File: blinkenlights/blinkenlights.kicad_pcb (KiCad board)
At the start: 4 copper layers, 160 x 100 mm, 169 parts, among them J201 Conn_03x32_Row_Letter_First, J301 Conn_01x01_Female, J302 Conn_01x01_Female, J303 Conn_01x01_Female, J304 Conn_01x01_Female, J501 Conn_ARM_SWD, J502 Conn_02x03_Odd_Even, SW101 Black, SW102 Orang, U104 74AUC2G07, U106 74HC2G14, U301 BD9C301FJ, U303 AMS1117-3.3, U401 74HC244, U402 74AUC2G34, U501 ATSAM4S8CB-AN, U502 PCA9306DP, U601 SN74LVCH16T245, U602 SN74LXC8T245, U603 SN74LVC2T45, U604 SN74LVC2T45, U605 SN74LVC2T45, U606 SN74LVCH16T245, U607 SN74LXC8T245, U608 74LVC2G06, U609 74LVC2G06, U610 74LVC2G06, U611 74LVC2G06

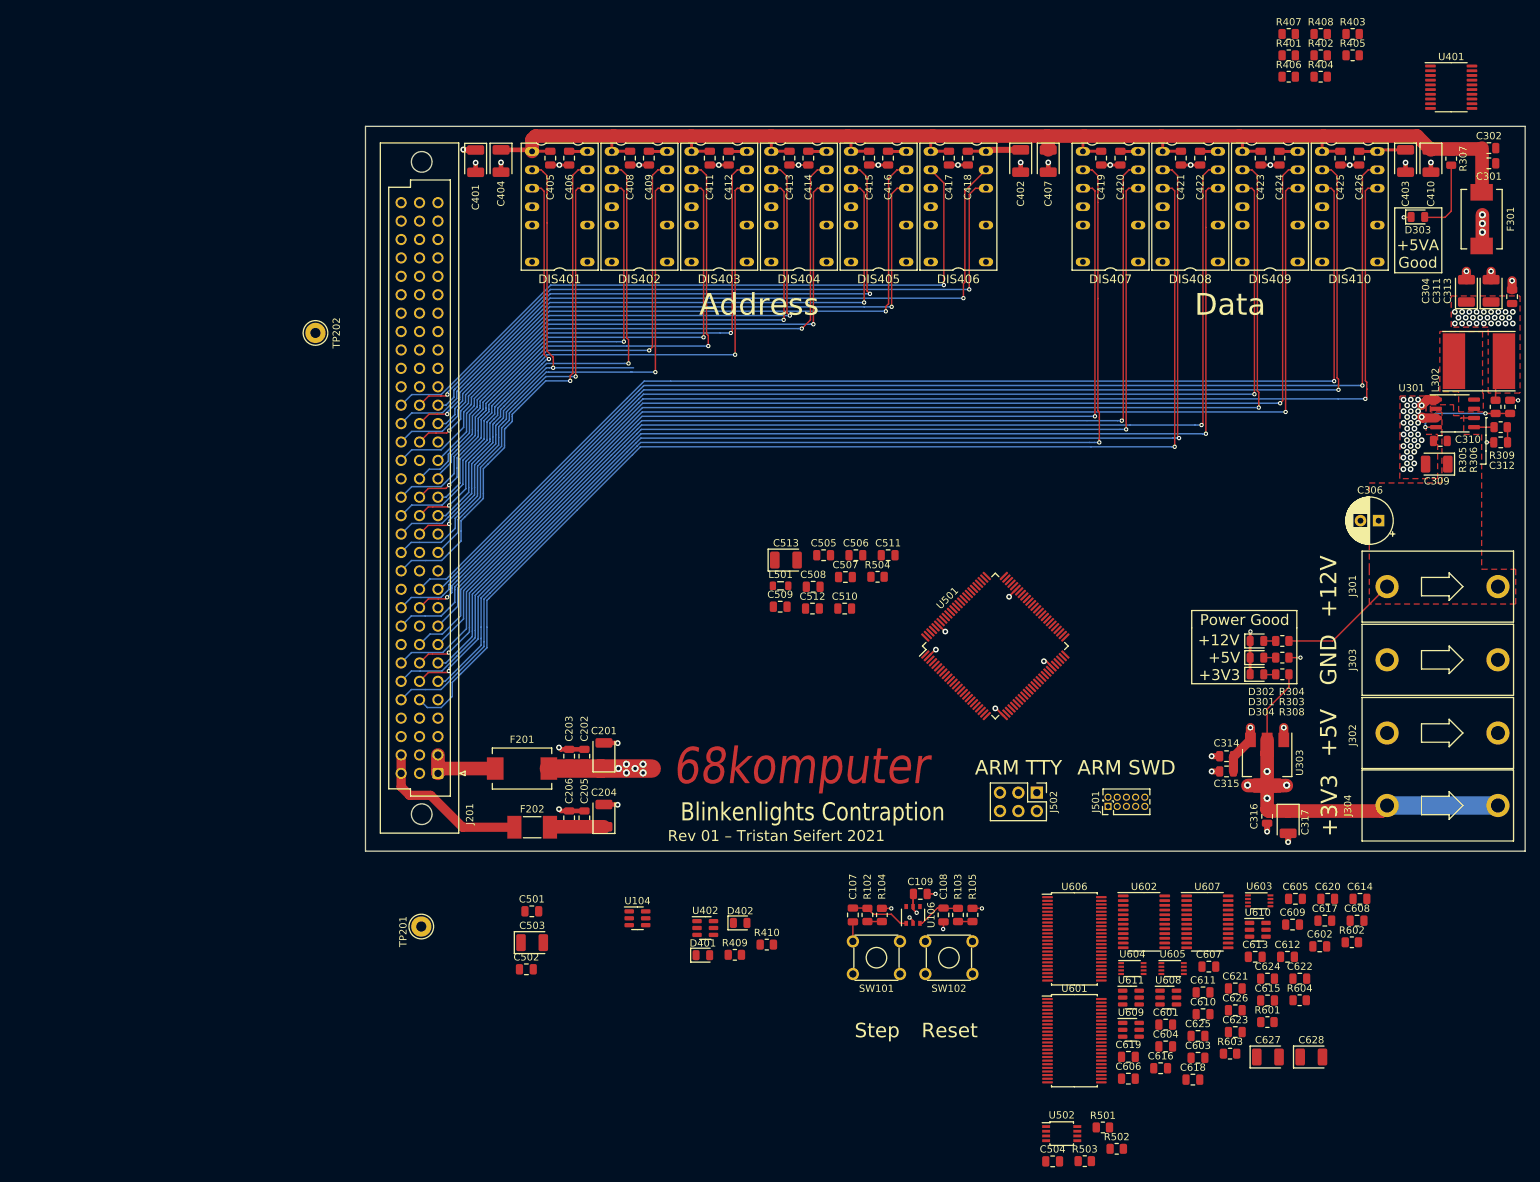
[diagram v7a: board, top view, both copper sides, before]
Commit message: Get rid of CPU on blinkenlights board
- We don't really care for having a full processor chilling on this
  board more than we do about being able to do a few bus transactions
  (to do fun stuff like flashing the boot ROMs) so we're going to put a
  bunch of SPI IO expanders instead; this should allow us to somewhat
  recreate bus cycles.

  We'll have to implement the run/halt/single step controls with
  dedicated logic though.
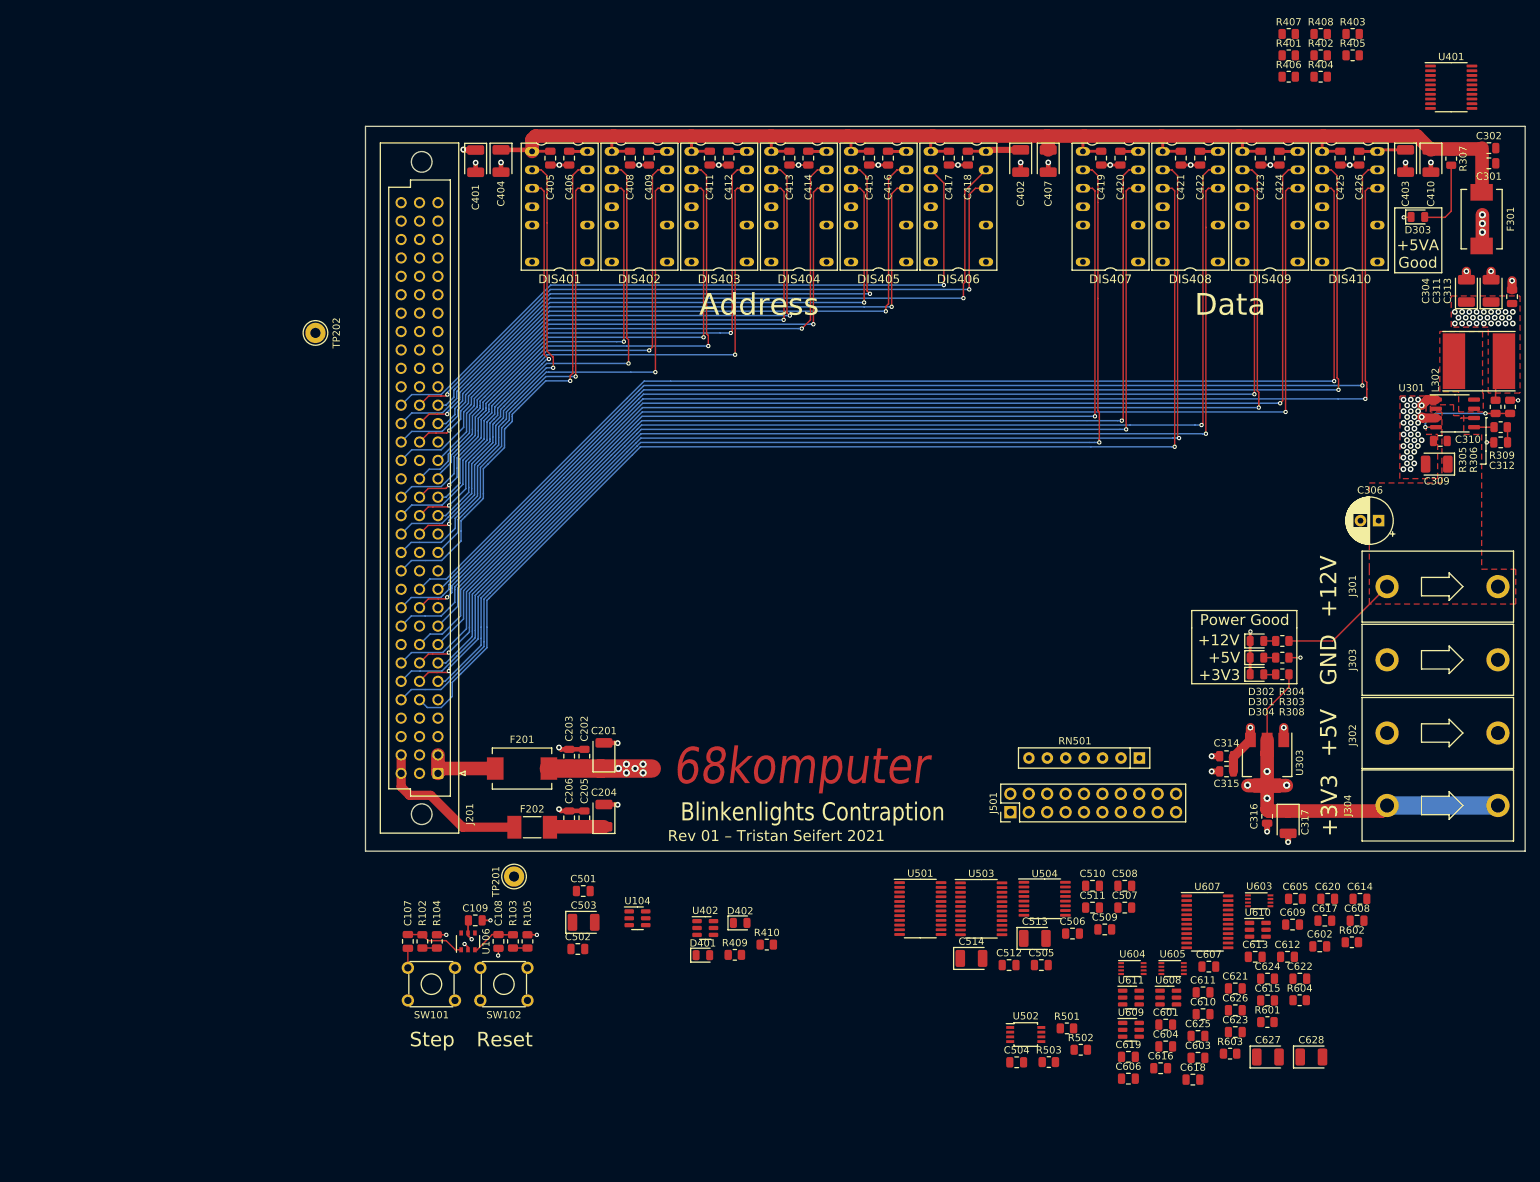
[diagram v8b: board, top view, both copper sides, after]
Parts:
- removed J502: Conn_02x03_Odd_Even, Connector_PinHeader_2.54mm:PinHeader_2x03_P2.54mm_Vertical
- removed L501: 10µH, Inductor_SMD:L_0805_2012Metric
- removed R504: 1R, Resistor_SMD:R_0805_2012Metric
- removed U601, U606: SN74LVCH16T245, Package_SO:TSSOP-48_6.1x12.5mm_P0.5mm
- removed U602: SN74LXC8T245, Package_SO:TSSOP-24_4.4x7.8mm_P0.65mm
- added C514: 10µF, Capacitor_Tantalum_SMD:CP_EIA-3528-21_Kemet-B, F.Cu at (103.6, 134.8)
- added RN501: 10k, Resistor_THT:R_Array_SIP7, F.Cu at (126.8, 107.2)
- added U503: XRA1403, Package_SO:TSSOP-24_4.4x7.8mm_P0.65mm, F.Cu at (105.0, 128.0)
- added U504: XRA1402, Package_SO:TSSOP-16_4.4x5mm_P0.65mm, F.Cu at (113.7, 126.6)
- C506, C510: value 100nF -> 4.7µF
- C509: value 4.7µF -> 100nF
- J501: value Conn_ARM_SWD -> Conn_02x10_Odd_Even; footprint Connector_PinHeader_1.27mm:PinHeader_2x05_P1.27mm_Vertical -> Connector_PinHeader_2.54mm:PinHeader_2x10_P2.54mm_Vertical
- U501: value ATSAM4S8CB-AN -> XRA1403; footprint Package_QFP:TQFP-100_14x14mm_P0.5mm -> Package_SO:TSSOP-24_4.4x7.8mm_P0.65mm
- moved C505 64.0 mm to (113.2, 135.7)
- moved C509 63.2 mm to (122.0, 130.8)
- moved C513 62.5 mm to (112.4, 132.0)
- moved C107 61.5 mm to (25.9, 132.4)
- moved C108 61.5 mm to (38.4, 132.4)
- moved C109 61.5 mm to (35.1, 129.6)
- moved R102 61.5 mm to (27.9, 132.4)
- moved R103 61.5 mm to (40.4, 132.4)
- moved R104 61.5 mm to (29.9, 132.4)
- moved R105 61.5 mm to (42.4, 132.4)
- moved SW101 61.5 mm to (25.9, 136.1)
- moved SW102 61.5 mm to (35.9, 136.1)
- moved U106 61.5 mm to (34.1, 132.4)
- moved C506 60.2 mm to (117.5, 131.4)
- moved C507 59.7 mm to (124.8, 127.8)
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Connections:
- net /Microcontroller/3V3_R/~{W} renamed /IO Drivers/3V3_R/~{W}
- net /Microcontroller/ADDR_DIR renamed /IO Drivers/Level Shifting/ADDR_DIR
- net /Microcontroller/BERR renamed /IO Drivers/BERR
- net /Microcontroller/BGACK renamed /IO Drivers/BGACK
- net /Microcontroller/BR renamed /IO Drivers/BR
- net /Microcontroller/DTACK renamed /IO Drivers/DTACK
- net /Microcontroller/HALT renamed /IO Drivers/HALT
- net /Microcontroller/I2C_IRQ renamed /IO Drivers/I2C_IRQ
- net /Microcontroller/I2C_SCL renamed /IO Drivers/I2C_SCL
- net /Microcontroller/I2C_SDA renamed /IO Drivers/I2C_SDA
- net /Microcontroller/IRQ renamed /IO Drivers/IRQ
- net /Microcontroller/RESET renamed /IO Drivers/RESET
- net /Microcontroller/R/~{W} renamed /IO Drivers/R/~{W}
- net /Microcontroller/~{3V3_AS} renamed /IO Drivers/~{3V3_AS}
- net /Microcontroller/~{3V3_BERR} renamed /IO Drivers/~{3V3_BERR}
- net /Microcontroller/~{3V3_BG} renamed /IO Drivers/~{3V3_BG}
- net /Microcontroller/~{3V3_DTACK} renamed /IO Drivers/~{3V3_DTACK}
- net /Microcontroller/~{3V3_HALT} renamed /IO Drivers/~{3V3_HALT}
- net /Microcontroller/~{3V3_IACK} renamed /IO Drivers/~{3V3_IACK}
- net /Microcontroller/~{3V3_LDS} renamed /IO Drivers/~{3V3_LDS}
- net /Microcontroller/~{3V3_MEM} renamed /IO Drivers/~{3V3_MEM}
- net /Microcontroller/~{3V3_RESET} renamed /IO Drivers/~{3V3_RESET}
- net /Microcontroller/~{3V3_UDS} renamed /IO Drivers/~{3V3_UDS}
- net /Microcontroller/~{AS} renamed /IO Drivers/~{AS}
- net /Microcontroller/~{BERR} renamed /IO Drivers/~{BERR}
- net /Microcontroller/~{BGACK} renamed /IO Drivers/~{BGACK}
- net /Microcontroller/~{BG} renamed /IO Drivers/~{BG}
- net /Microcontroller/~{BR} renamed /IO Drivers/~{BR}
- net /Microcontroller/~{DTACK} renamed /IO Drivers/~{DTACK}
- net /Microcontroller/~{HALT} renamed /IO Drivers/~{HALT}
- net /Microcontroller/~{I2C_IRQ} renamed /IO Drivers/~{I2C_IRQ}
- net /Microcontroller/~{IACK} renamed /IO Drivers/~{IACK}
- net /Microcontroller/~{IRQ} renamed /IO Drivers/~{IRQ}
- net /Microcontroller/~{LDS} renamed /IO Drivers/~{LDS}
- net /Microcontroller/~{MEM} renamed /IO Drivers/~{MEM}
- net /Microcontroller/~{RESET} renamed /IO Drivers/~{RESET}
- net /Microcontroller/~{UDS} renamed /IO Drivers/~{UDS}
- C505 pad 1: VDDCORE -> +3V3
- C506 pad 1: Net-(C506-Pad1) -> +3V3
- C507 pad 1: VDDCORE -> +3V3
- C508 pad 1: Net-(C508-Pad1) -> +3V3
- C509 pad 1: VDDCORE -> +3V3
- J501 pad 1: +3V3 -> /IO Drivers/~{TST_RESET}
- J501 pad 10: /Microcontroller/~{SWD_NRST} -> /IO Drivers/~{IO2_CS}
- J501 pad 2: /Microcontroller/JTAG_TMS -> GND
- J501 pad 3: GND -> /IO Drivers/SCK
- J501 pad 4: /Microcontroller/JTAG_TCK -> /IO Drivers/MOSI
- J501 pad 5: GND -> /IO Drivers/~{TST_IRQ}
- J501 pad 6: /Microcontroller/JTAG_TDO -> /IO Drivers/MISO
- J501 pad 7: unconnected-(J501-Pad7) -> GND
- J501 pad 8: /Microcontroller/JTAG_TDI -> /IO Drivers/~{IO1_CS}
- J501 pad 9: GND -> /IO Drivers/SCL
- R502 pad 1: /Microcontroller/SDA -> /IO Drivers/SDA
- R503 pad 1: /Microcontroller/SCL -> /IO Drivers/SCL
- R602 pad 1: /Microcontroller/~{ADDR_OE} -> /IO Drivers/Level Shifting/~{ADDR_OE}
- R603 pad 1: /Microcontroller/DATA_DIR -> /IO Drivers/Level Shifting/DATA_DIR
- R604 pad 1: /Microcontroller/~{DATA_OE} -> /IO Drivers/Level Shifting/~{DATA_OE}
- U501 pad 1: unconnected-(U501-Pad1) -> /IO Drivers/~{TST_IRQ}
- U501 pad 10: +3V3 -> unconnected-(U501-Pad10)
- U501 pad 11: VDDCORE -> unconnected-(U501-Pad11)
- U501 pad 12: unconnected-(U501-Pad12) -> GND
- U501 pad 16: VDDCORE -> unconnected-(U501-Pad16)
- U501 pad 2: GND -> /IO Drivers/MOSI
- U501 pad 21: unconnected-(U501-Pad21) -> /IO Drivers/~{IO1_CS}
- U501 pad 22: unconnected-(U501-Pad22) -> /IO Drivers/SCK
- U501 pad 23: unconnected-(U501-Pad23) -> /IO Drivers/MISO
- U501 pad 24: unconnected-(U501-Pad24) -> +3V3
- U501 pad 3: unconnected-(U501-Pad3) -> /IO Drivers/~{TST_RESET}
- U502 pad 3: /Microcontroller/SCL -> /IO Drivers/SCL
- U502 pad 4: /Microcontroller/SDA -> /IO Drivers/SDA
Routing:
- net /A21: track 73.1 -> 62.0 mm
- net GND: track 81.2 -> 74.1 mm, vias 74 -> 69
- net +3V3: track 60.7 -> 57.5 mm
- net /A5: track 86.0 -> 85.4 mm
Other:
- board text removed: "ARM SWD"
- board text removed: "ARM TTY"
